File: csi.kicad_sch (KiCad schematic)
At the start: 65 parts, among them J7 Conn_FFC_WE_68715014522, J8 Conn_FFC_WE_68715014522, U24 AP22615A_TSOT26, U25 AP22615A_TSOT26, U26 PI4MSD5V9548AZDEX, U27 AP22615A_TSOT26, U28 AP22615A_TSOT26, U31 NTS0102_XSON, U32 NTS0102_XSON

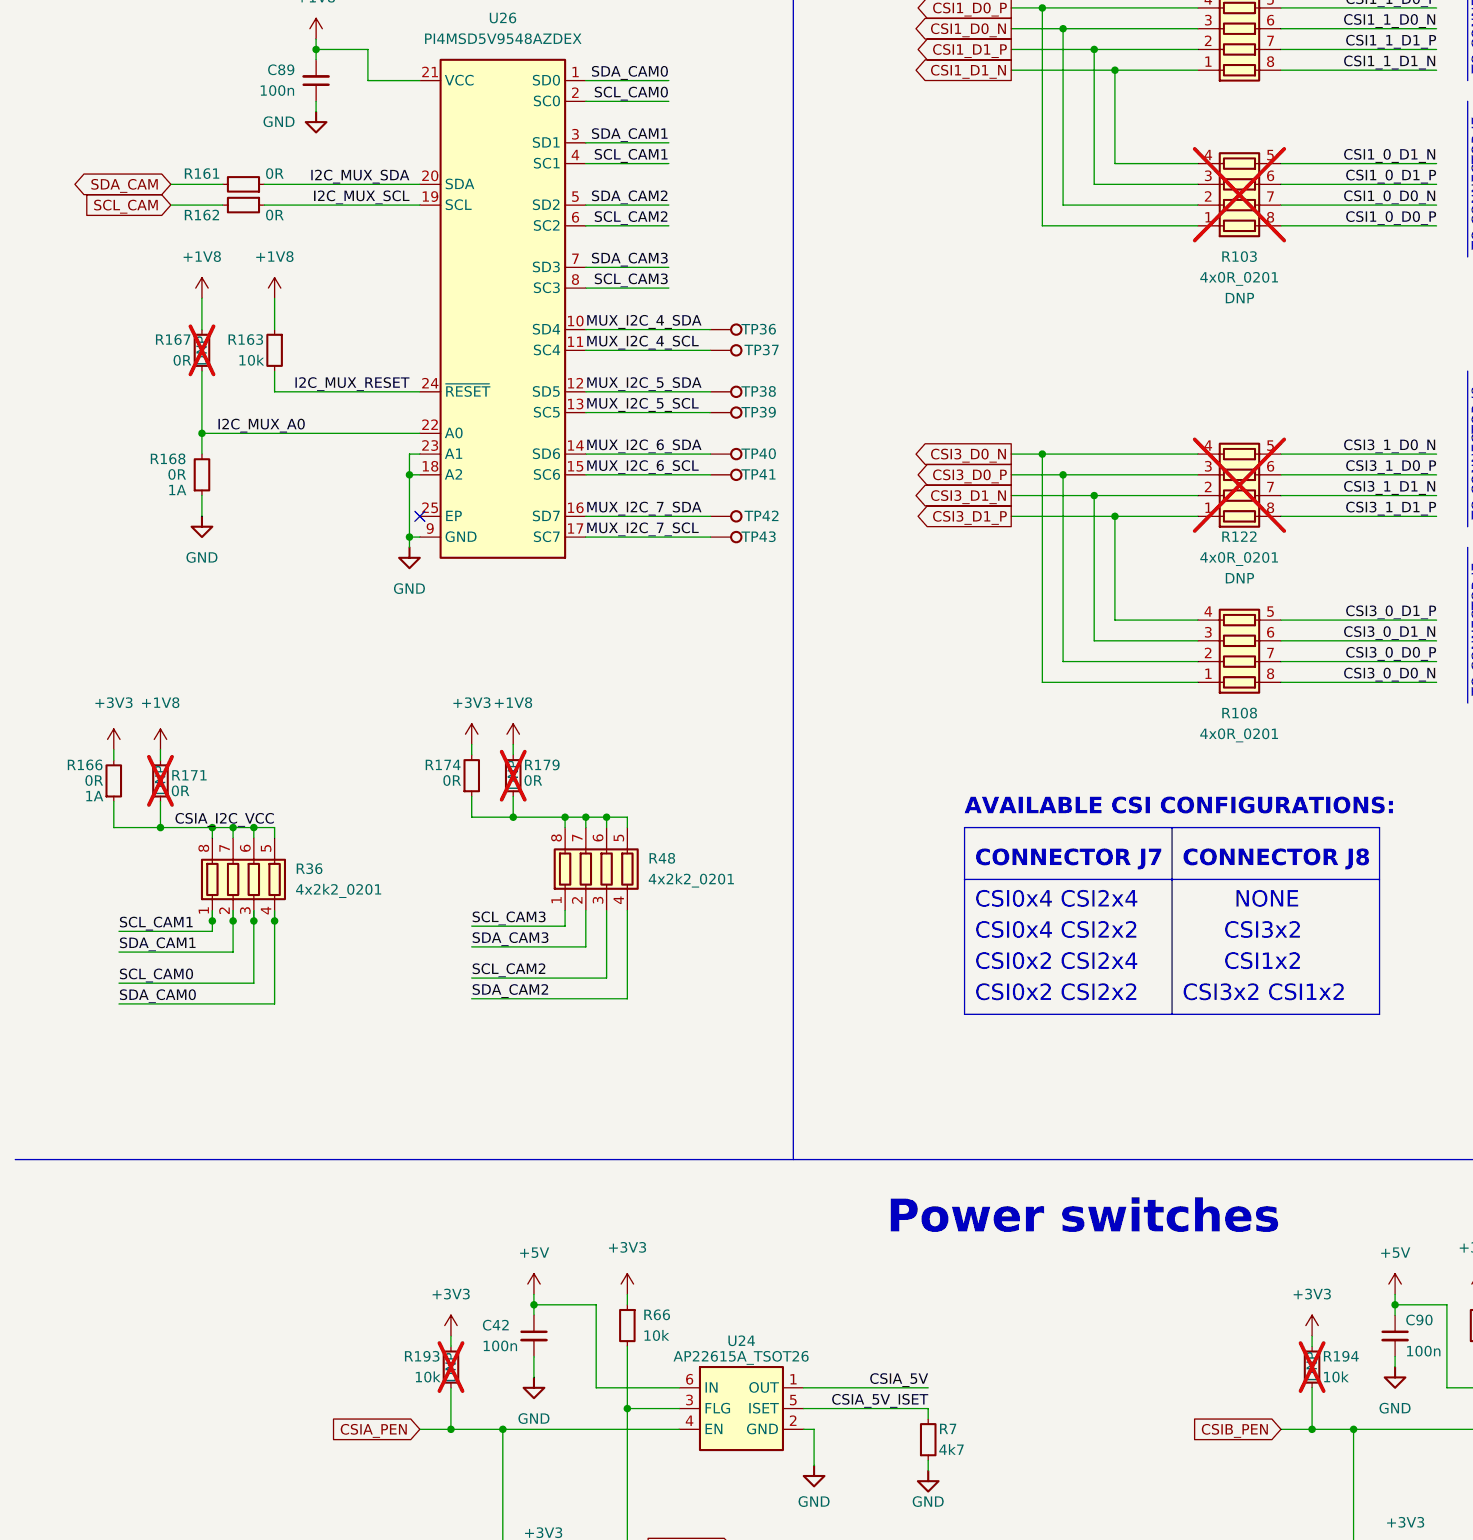
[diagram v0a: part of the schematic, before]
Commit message: 5/16 Commit: Sch Mods added and beginning Development on PCB layout
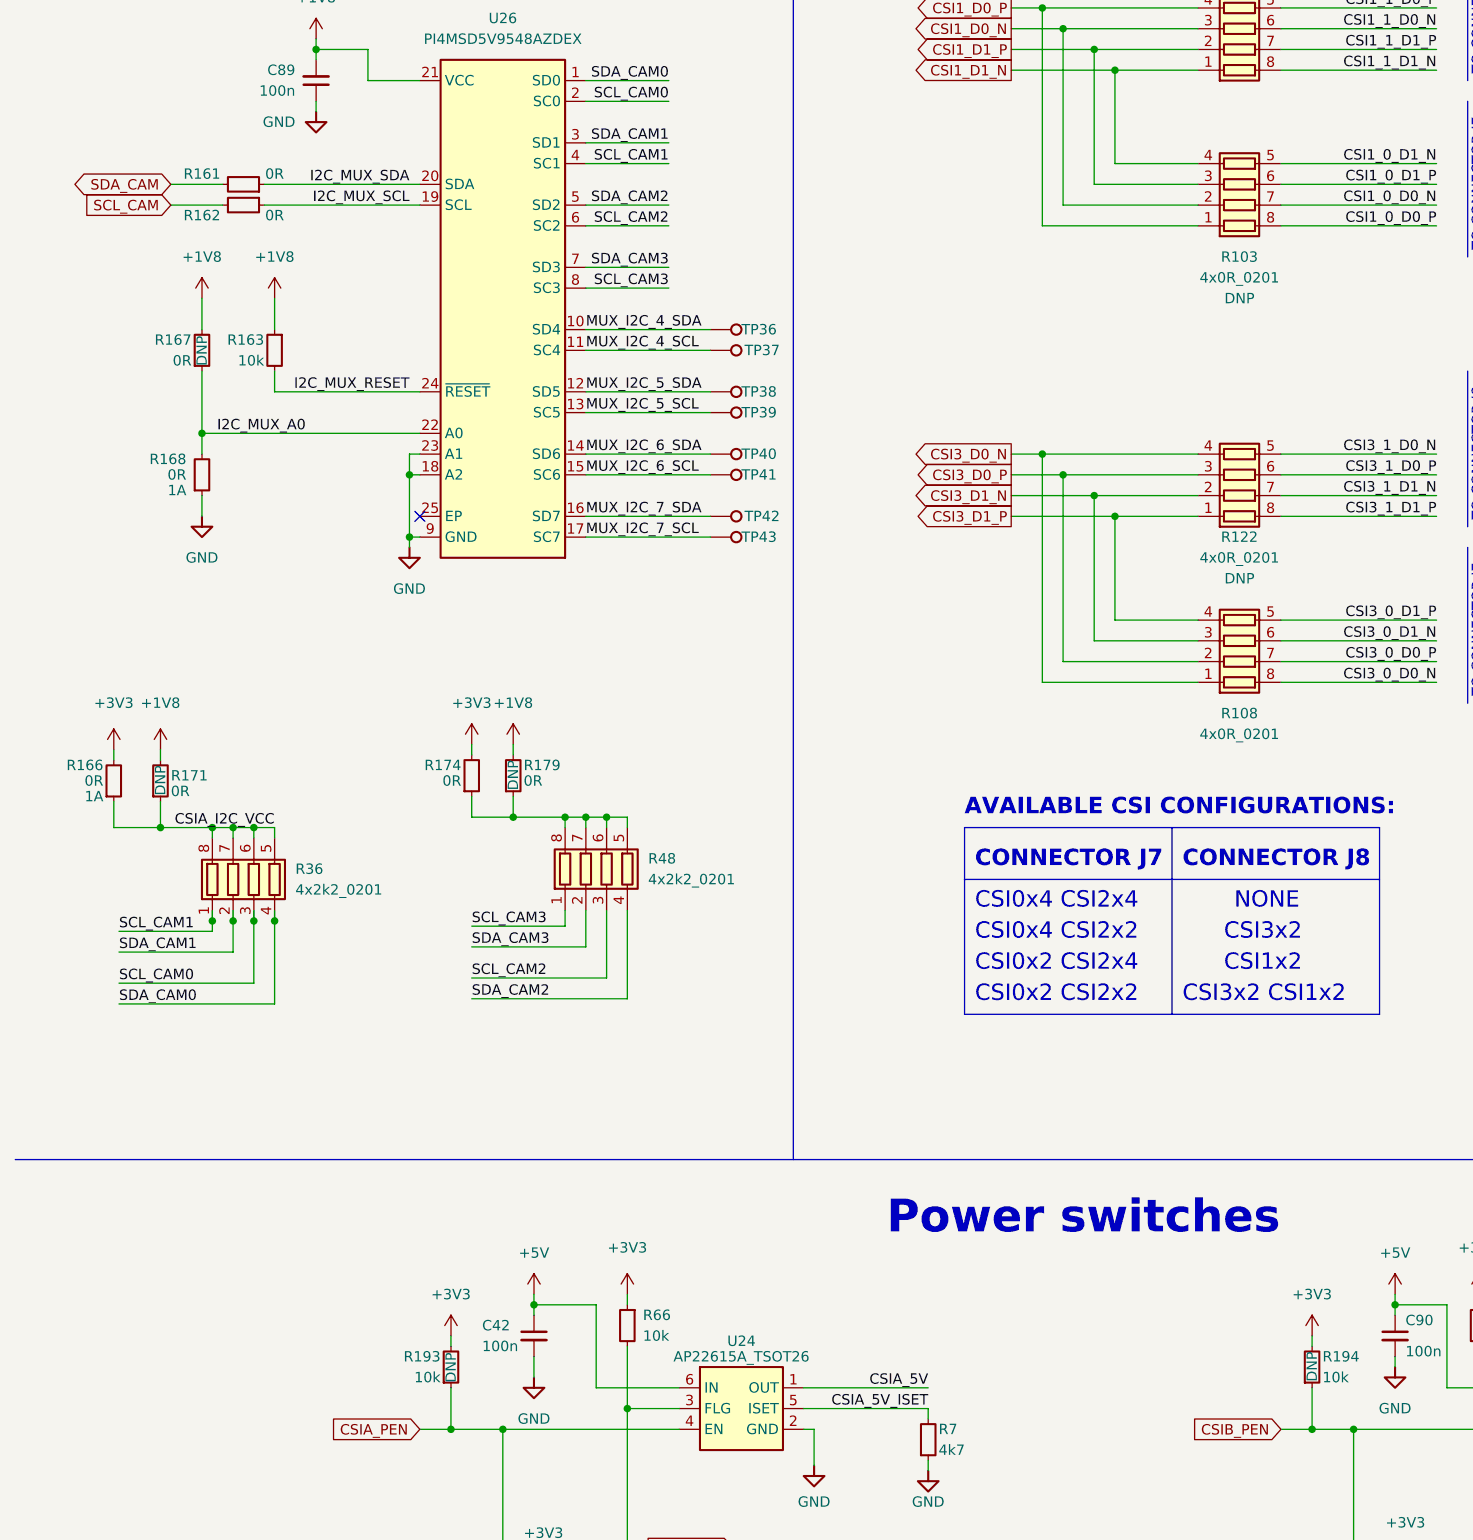
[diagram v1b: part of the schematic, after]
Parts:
- R103, R122, R167, R171, R179, R193, R194: now fitted
